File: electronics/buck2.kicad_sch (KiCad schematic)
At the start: 14 parts, among them U3 TPS54302DDCR

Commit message: Integrate onboard RP2040 and drawing-based EV3 jacks on A1 PCB
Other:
- title: Quadcuber A0 / buck2 / ENGINEERING HOLD -> Quadcuber A1 / buck2 / ENGINEERING HOLD

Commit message: Correct audited power BOM and add bounded VM discharge protection
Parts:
- C30: MPN GRM32ER71E106KA12L -> GRM32DR71E106KA12L
- C35: MPN GRM1885C1H750JA01D -> C0603C750J5GACTU; Manufacturer Murata -> KEMET

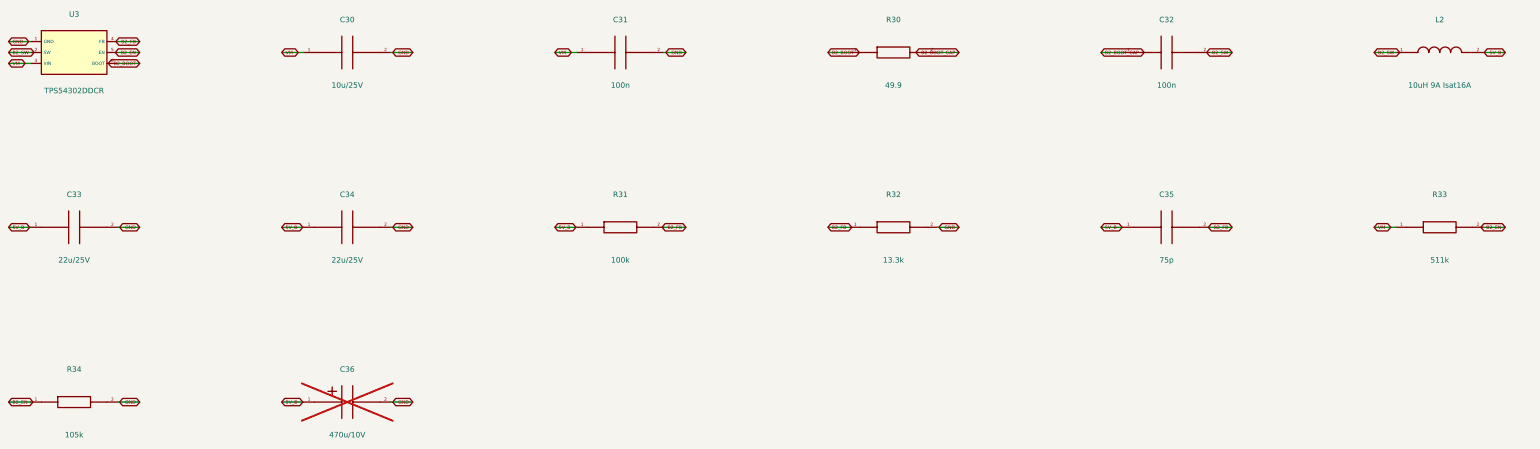
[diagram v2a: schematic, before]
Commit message: Migrate A1 to KiCad 10 and record blocked vendor-model transients
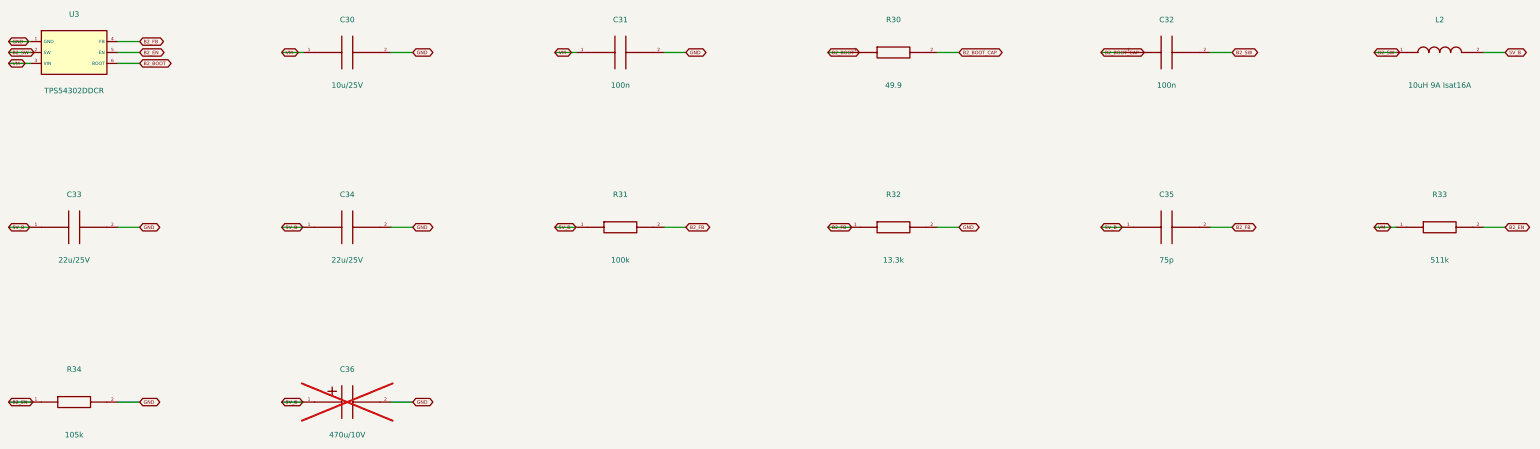
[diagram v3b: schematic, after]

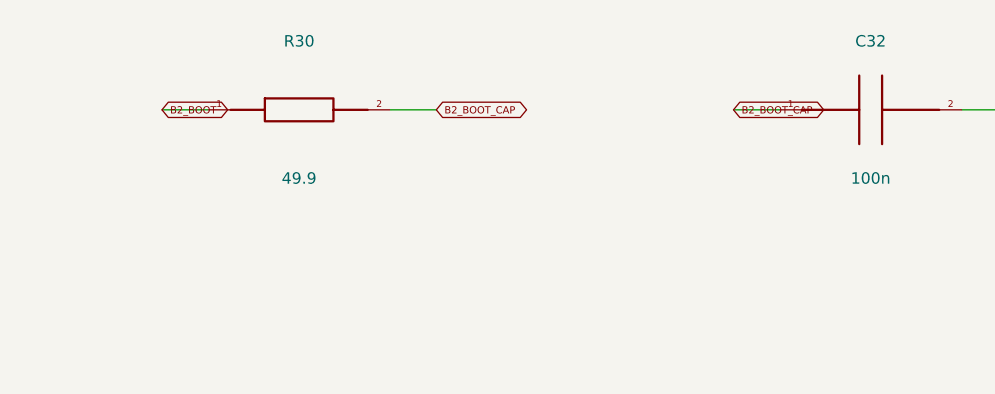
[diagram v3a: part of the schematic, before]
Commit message: Correct A1 bootstrap routing and precision feedback with verified artifacts
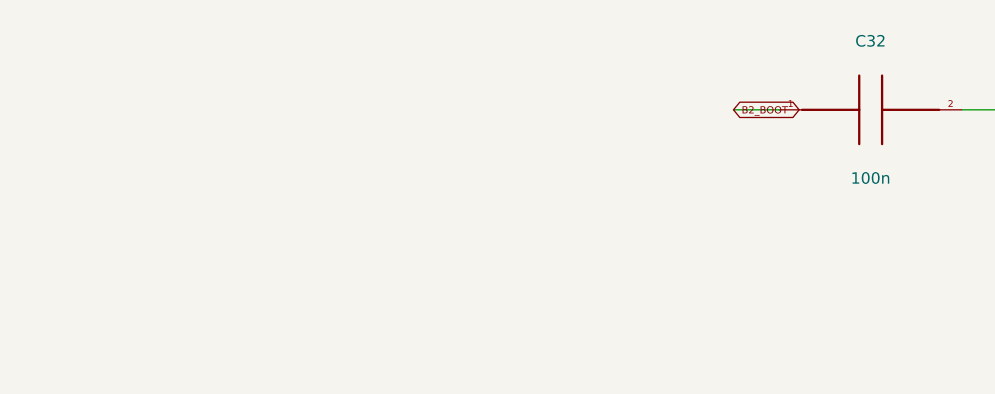
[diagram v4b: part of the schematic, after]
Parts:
- removed R30: 49.9, Quadcuber:R_0603_1608Metric, symbol Quadcuber:R30
- R31: MPN RC0603FR-07100KL -> RT0603BRD07100KL
- R32: MPN RC0603FR-0713K3L -> RT0603BRD0713K3L
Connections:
- net B2_BOOT_CAP is gone; now on net B2_BOOT: C32.1
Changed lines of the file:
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@@
-	(wire
-		(pts
-			(xy 236.22 38.1) (xy 241.3 38.1)
-		)
-		(stroke
-			(width 0)
-			(type default)
-		)
-	)
 	(wire
 		(pts
@@
 	(wire
 		(pts
-			(xy 215.9 38.1) (xy 210.82 38.1)
-		)
-		(stroke
-			(width 0)
-			(type default)
-		)
-	)
-	(wire
-		(pts
 			(xy 109.22 38.1) (xy 114.3 38.1)
 		)
@@
 		)
 	)
-	(global_label "B2_BOOT_CAP"
-		(shape bidirectional)
-		(at 241.3 38.1 0)
-		(effects
-			(font
-				(size 0.8 0.8)
-			)
-		)
-		(property "Intersheetrefs" "${INTERSHEET_REFS}"
-			(at 241.3 38.1 180)
-			(hide yes)
-			(show_name no)
-			(do_not_autoplace no)
-			(effects
-				(font
-					(size 0.8 0.8)
-				)
-			)
-		)
-	)
 	(global_label "5V_B"
 		(shape bidirectional)
@@
 		)
 	)
+	(global_label "GND"
+		(shape bidirectional)
+		(at 50.8 119.38 0)
+		(effects
+			(font
+				(size 0.8 0.8)
+			)
+		)
+		(property "Intersheetrefs" "${INTERSHEET_REFS}"
+			(at 50.8 119.38 180)
+			(hide yes)
+			(show_name no)
+			(do_not_autoplace no)
+			(effects
+				(font
+					(size 0.8 0.8)
+				)
+			)
+		)
+	)
+	(global_label "B2_SW"
+		(shape bidirectional)
+		(at 20.32 38.1 0)
+		(effects
+			(font
+				(size 0.8 0.8)
+			)
+		)
+		(property "Intersheetrefs" "${INTERSHEET_REFS}"
+			(at 20.32 38.1 0)
+			(hide yes)
+			(show_name no)
+			(do_not_autoplace no)
+			(effects
+				(font
+					(size 0.8 0.8)
+				)
+			)
+		)
+	)
+	(global_label "GND"
+		(shape bidirectional)
+		(at 114.3 78.74 0)
+		(effects
+			(font
+				(size 0.8 0.8)
+			)
+		)
+		(property "Intersheetrefs" "${INTERSHEET_REFS}"
+			(at 114.3 78.74 180)
+			(hide yes)
+			(show_name no)
+			(do_not_autoplace no)
+			(effects
+				(font
+					(size 0.8 0.8)
+				)
+			)
+		)
+	)
+	(global_label "5V_B"
+		(shape bidirectional)
+		(at 274.32 78.74 0)
+		(effects
+			(font
+				(size 0.8 0.8)
+			)
+		)
+		(property "Intersheetrefs" "${INTERSHEET_REFS}"
+			(at 274.32 78.74 0)
+			(hide yes)
+			(show_name no)
+			(do_not_autoplace no)
+			(effects
+				(font
+					(size 0.8 0.8)
+				)
+			)
+		)
+	)
 	(global_label "B2_BOOT"
-		(shape bidirectional)
-		(at 210.82 38.1 0)
-		(effects
-			(font
-				(size 0.8 0.8)
-			)
-		)
-		(property "Intersheetrefs" "${INTERSHEET_REFS}"
-			(at 210.82 38.1 0)
-			(hide yes)
-			(show_name no)
-			(do_not_autoplace no)
-			(effects
-				(font
-					(size 0.8 0.8)
-				)
-			)
-		)
-	)
-	(global_label "GND"
-		(shape bidirectional)
-		(at 50.8 119.38 0)
-		(effects
-			(font
-				(size 0.8 0.8)
-			)
-		)
-		(property "Intersheetrefs" "${INTERSHEET_REFS}"
-			(at 50.8 119.38 180)
-			(hide yes)
-			(show_name no)
-			(do_not_autoplace no)
-			(effects
-				(font
-					(size 0.8 0.8)
-				)
-			)
-		)
-	)
-	(global_label "B2_SW"
-		(shape bidirectional)
-		(at 20.32 38.1 0)
-		(effects
-			(font
-				(size 0.8 0.8)
-			)
-		)
-		(property "Intersheetrefs" "${INTERSHEET_REFS}"
-			(at 20.32 38.1 0)
-			(hide yes)
-			(show_name no)
-			(do_not_autoplace no)
-			(effects
-				(font
-					(size 0.8 0.8)
-				)
-			)
-		)
-	)
-	(global_label "GND"
-		(shape bidirectional)
-		(at 114.3 78.74 0)
-		(effects
-			(font
-				(size 0.8 0.8)
-			)
-		)
-		(property "Intersheetrefs" "${INTERSHEET_REFS}"
-			(at 114.3 78.74 180)
-			(hide yes)
-			(show_name no)
-			(do_not_autoplace no)
-			(effects
-				(font
-					(size 0.8 0.8)
-				)
-			)
-		)
-	)
-	(global_label "5V_B"
-		(shape bidirectional)
-		(at 274.32 78.74 0)
-		(effects
-			(font
-				(size 0.8 0.8)
-			)
-		)
-		(property "Intersheetrefs" "${INTERSHEET_REFS}"
-			(at 274.32 78.74 0)
-			(hide yes)
-			(show_name no)
-			(do_not_autoplace no)
-			(effects
-				(font
-					(size 0.8 0.8)
-				)
-			)
-		)
-	)
-	(global_label "B2_BOOT_CAP"
 		(shape bidirectional)
 		(at 274.32 38.1 0)
@@
 			)
 		)
-		(property "MPN" "RC0603FR-0713K3L"
+		(property "MPN" "RT0603BRD0713K3L"
 			(at 226.06 78.74 0)
 			(hide yes)
@@
 			)
 		)
-		(property "MPN" "RC0603FR-07100KL"
+		(property "MPN" "RT0603BRD07100KL"
 			(at 162.56 78.74 0)
 			(hide yes)
@@
 					(unit 1)
 				)
-			)
-		)
-	)
-	(symbol
-		(lib_id "Quadcuber:R30")
-		(at 226.06 38.1 0)
-		(unit 1)
-		(body_style 1)
-		(exclude_from_sim no)
-		(in_bom yes)
-		(on_board yes)
-		(in_pos_files yes)
-		(dnp no)
-		(property "Reference" "R30"
-			(at 226.06 30.48 0)
-			(show_name no)
-			(do_not_autoplace no)
-			(effects
-				(font
-					(size 1.27 1.27)
-				)
-			)
-		)
-		(property "Value" "49.9"
-			(at 226.06 45.72 0)
-			(show_name no)
-			(do_not_autoplace no)
-			(effects
-				(font
-					(size 1.27 1.27)
-				)
-			)
-		)
-		(property "Footprint" "Quadcuber:R_0603_1608Metric"
-			(at 226.06 38.1 0)
-			(hide yes)
-			(show_name no)
-			(do_not_autoplace no)
-			(effects
-				(font
-					(size 1.27 1.27)
-				)
-			)
-		)
-		(property "Datasheet" ""
-			(at 226.06 38.1 0)
-			(show_name no)
-			(do_not_autoplace no)
-			(effects
-				(font
-					(size 1.27 1.27)
-				)
-			)
-		)
-		(property "Description" ""
-			(at 226.06 38.1 0)
-			(show_name no)
-			(do_not_autoplace no)
-			(effects
-				(font
-					(size 1.27 1.27)
-				)
-			)
-		)
-		(property "MPN" "RC0603FR-0749R9L"
-			(at 226.06 38.1 0)
-			(hide yes)
-			(show_name no)
-			(do_not_autoplace no)
-			(effects
-				(font
-					(size 1.27 1.27)
-				)
-			)
-		)
-		(property "Manufacturer" "Yageo"
-			(at 226.06 38.1 0)
-			(hide yes)
-			(show_name no)
-			(do_not_autoplace no)
-			(effects
-				(font
-					(size 1.27 1.27)
-				)
-			)
-		)
-		(pin "1"
-		)
-		(pin "2"
-		)
-		(instances
-			(project "quadcuber"
-				(path "/822f0fe2-7874-52bf-b949-33e1d201f157/e8b2a047-8402-5099-87d9-9604c9e31a0c"
-					(reference "R30")
-					(unit 1)
-				)
